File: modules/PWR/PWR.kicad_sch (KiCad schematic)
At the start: 18 parts, among them SW1 POWER ON, SW2 RESET, U1 74HC00

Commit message: pwr pcb
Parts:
- R1: value 150Ω -> 1kΩ
- R2: value 100Ω -> 1kΩ
- U1: value 74HC00 -> 74HCT00
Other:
- note added: "BUS RESET"
- note added: "I^{2}C SUPPORT"
- note added: "METERS"
- note added: "POWER AND DECOUPLING"
- note added: "POWER CONTROL"
- note added: "TURNS OFF THE STANDBY LED WHEN MAIN POWER IS ENABLED."
- title: PWR-CTRL -> PWR
- moved on the sheet: C1, C2, C3, D1, D2, JP1, MES1, MES2, MES3, MES4, R1, R2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

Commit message: minor PW PCB tweaks
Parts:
- SW1: value POWER ON -> PWR ON
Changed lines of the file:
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@@
 			)
 		)
-		(property "Value" "POWER ON"
+		(property "Value" "PWR ON"
 			(at 77.47 35.56 0)
 			(show_name no)

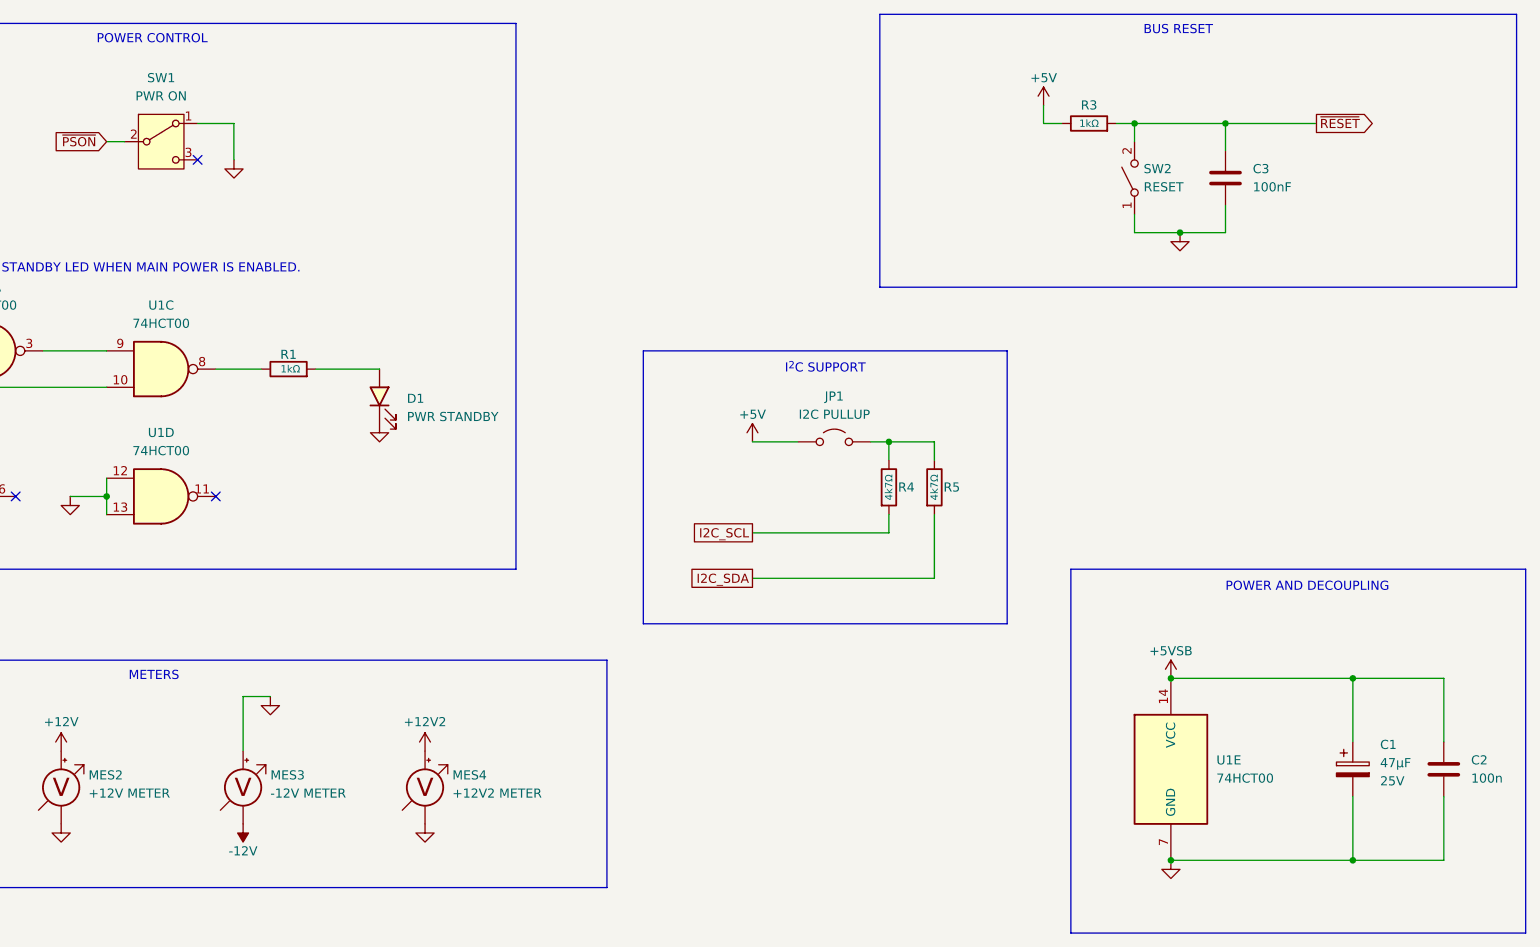
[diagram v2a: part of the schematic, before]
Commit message: version 1 of pwr module, power panel, & backplane pcb
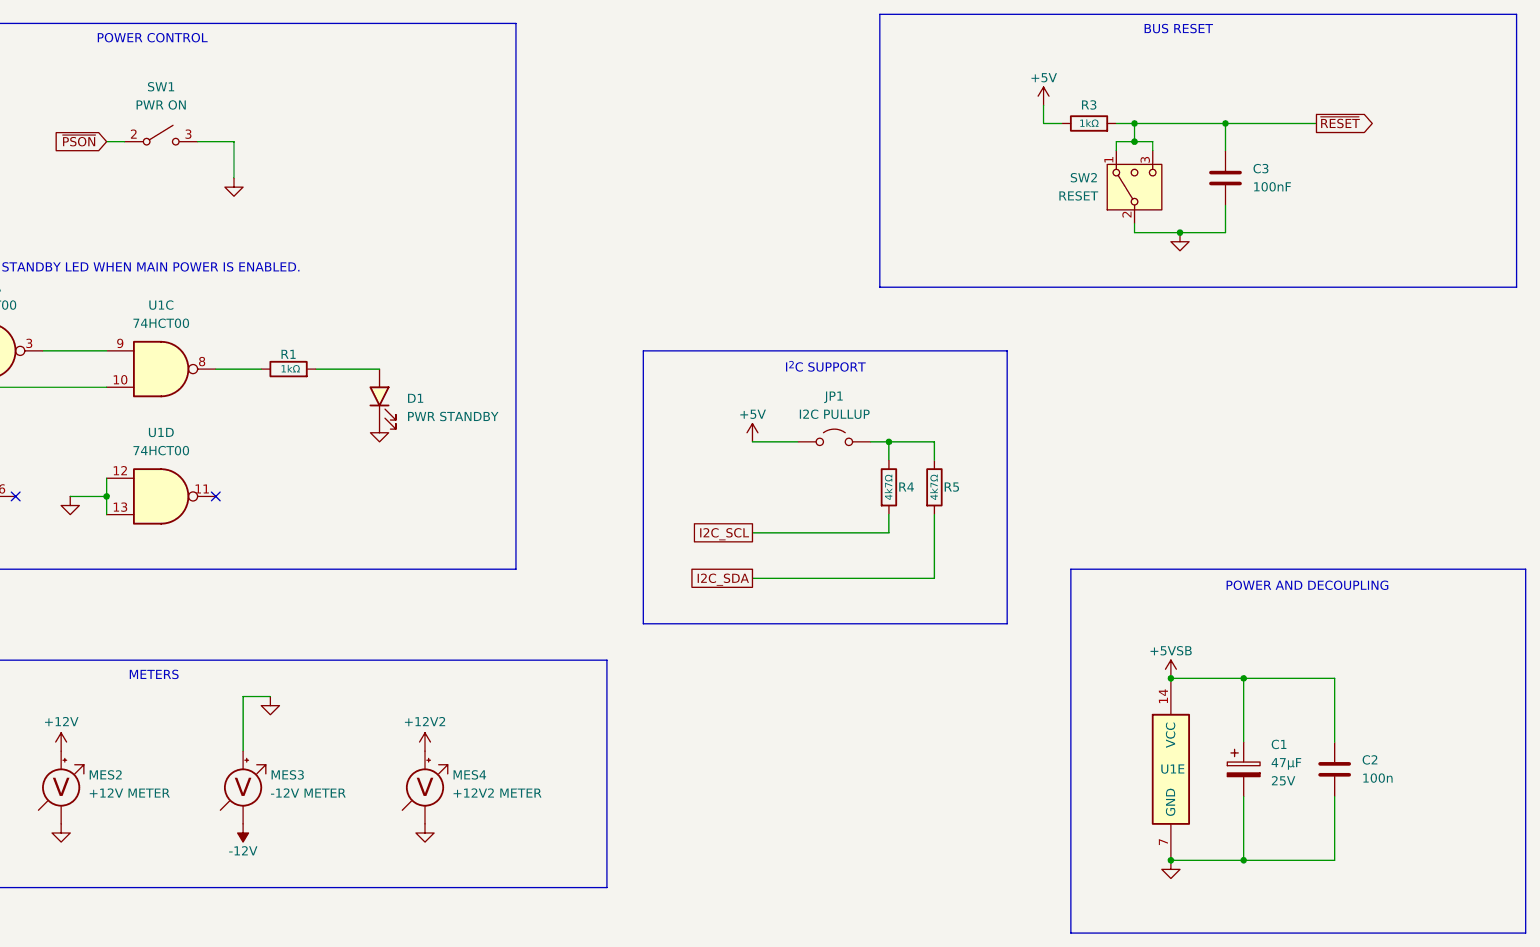
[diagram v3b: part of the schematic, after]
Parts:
- C1: footprint Capacitor_THT:CP_Radial_D5.0mm_P2.50mm -> FormantKO:CP_Radial_Tantal_P200mil
- D1, D2, MES1, MES2, MES3, MES4: footprint FormantKO:PanelConnector_1x02 -> IMNOTWOPR:PanelConnector_1x02
- JP1: footprint FormantKO:Jumper_1x02 -> IMNOTWOPR:Jumper_1x02
- SW1: footprint FormantKO:PanelConnector_1x02 -> IMNOTWOPR:PanelConnector_1x03; symbol Switch:SW_SPDT -> IMNOTWOPR:SW_SPST
- SW2: footprint FormantKO:PanelConnector_1x02 -> IMNOTWOPR:PanelConnector_1x03; symbol Switch:SW_SPST -> IMNOTWOPR:SW_SPDT_MSM
- U1: symbol 74xx:74HC00 -> IMNOTWOPR:74HCT00
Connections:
- net GND: now also SW1.3 (C), SW2.2 (3); no longer SW1.1 (A), SW2.1 (A)
- net ~{RESET}: now also SW2.1, SW2.3 (4); no longer SW2.2 (B)
- no-connect marks 3 -> 2
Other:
- moved on the sheet: C1, C2

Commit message: lib work and ben wip
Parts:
- removed R3: 1kΩ, IMNOTWOPR:R_Axial_DIN0207_P400mil, symbol IMNOTWOPR:R
- removed SW2: RESET, IMNOTWOPR:PanelConnector_1x03, symbol IMNOTWOPR:SW_SPDT_MSM
- added C1: 10n, IMNOTWOPR:C_Rect_P200mil, symbol IMNOTWOPR:C
- added C2: 1u, IMNOTWOPR:C_Rect_P200mil, symbol IMNOTWOPR:C
- added C6, C7: 100n, IMNOTWOPR:C_Rect_P200mil, symbol IMNOTWOPR:C
- added D2, D4: 1N4148, FormantKO:DO-35_P400mil, symbol IMNOTWOPR:1N4148
- added J1: CardConnector, IMNOTWOPR:SystemConector_Male, symbol IMNOTWOPR:CardConnector
- added MH1: CardBracket, IMNOTWOPR:CardBracket, symbol IMNOTWOPR:CardBracket
- added R2: 10k, IMNOTWOPR:R_Axial_DIN0207_P400mil, symbol IMNOTWOPR:R_Vertical
- added R3: 91k, IMNOTWOPR:R_Axial_DIN0207_P400mil, symbol IMNOTWOPR:R_Vertical
- added SW1: 1MS2T1B1M1QES, IMNOTWOPR:PanelConnector_1x03, symbol IMNOTWOPR:SW_SPST
- added U1: 74HCT14, IMNOTWOPR:DIP-14N, symbol IMNOTWOPR:74HCT14
- added U3: 555, IMNOTWOPR:DIP-8N, symbol IMNOTWOPR:555
- C3: value 100nF -> 10n
- C4: renamed from C1; footprint FormantKO:CP_Radial_Tantal_P200mil -> IMNOTWOPR:CP_Radial_Tantal_P100mil; Voltage 25V -> 35V
- D1: renamed from D2; footprint IMNOTWOPR:PanelConnector_1x02 -> IMNOTWOPR:LED_G_D5.0mm
- D3: renamed from D1; footprint IMNOTWOPR:PanelConnector_1x02 -> IMNOTWOPR:LED_D5.0mm
- JP1: footprint IMNOTWOPR:Jumper_1x02 -> (none)
- MES1, MES2, MES3, MES4: footprint IMNOTWOPR:PanelConnector_1x02 -> (none)
- SW2: renamed from SW1; value PWR ON -> 1MS1T1B1M1QES; Legend (none) -> POWER ON
- renumbered C2 to C5, R2 to R1, R1 to R4, R4 to R5, R5 to R6, U1 to U2
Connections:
- net +12V: now also J1.a3 (+12V), J1.a30 (+12V)
- net +12V2: now also J1.c3 (+12V2), J1.c30 (+12V2)
- net +5V: now also D2.1 (K), J1.a1 (+5V), J1.a2 (+5V), J1.a31 (+5V), J1.a32 (+5V), J1.b1 (+5V), J1.b32 (+5V), R2.2, R3.2, U3.4 (~{RST}), U3.8 (VCC)
- net +5VSB: now also C6.1, C7.1, J1.c1 (+5VSB), U1.14 (VCC)
- net -12V: now also J1.b3 (-12V), J1.b30 (-12V)
- net GND: now also C2.2, C6.2, C7.2, J1.b2 (GND), J1.b31 (GND), J1.c12 (GND), J1.c18 (GND), J1.c2 (GND), J1.c24 (GND), J1.c31 (GND), J1.c32 (GND), J1.c6 (GND), SW1.2 (B), U1.11, U1.13, U1.5, U1.7 (GND), U1.9, U3.1 (GND)
- net I2C_SCL: now also J1.c7 (I2C_SCL)
- net I2C_SDA: now also J1.c8 (I2C_SDA)
- net PWROK: now also J1.c5 (PWROK), U1.1
- net ~{PSON}: now also J1.c4 (~{PSON})
- net ~{RESET}: now also D4.1 (K), J1.b15 (~{RESET}); no longer C3.1
- new net: C1.1, U1.2
- new net: C1.2, D2.2 (A), R2.1, SW1.3 (C), U3.2 (TRIG)
- new net: C2.1, R3.1, U3.6 (THRES), U3.7 (DISCH)
- new net: U1.3, U3.3 (OUT)
- new net: C3.1, U3.5 (CONT)
- new net: D4.2 (A), U1.4
- no-connect marks 2 -> 75
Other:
- note added: "MANUAL & POWER ON RESET"
- note added: "≈ 100ms PULSE"
- note removed: "BUS RESET"
- moved on the sheet: C4, C5, D1, D3, JP1, MES1, MES2, MES3, MES4, R1, R4, R5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

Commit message: ben work; fixed logic issue with pwr; started lightman
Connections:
- net GND: no longer U2.4, U2.5
- net at U2.8: now also U2.4, U2.5; no longer R4.1
- net at U2.6: now also R4.1
- no-connect marks 75 -> 74
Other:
- moved on the sheet: D3, R4
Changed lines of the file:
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@@
 	)
 	(junction
-		(at 81.28 255.27)
+		(at 133.35 73.66)
 		(diameter 0)
 		(color 0 0 0 0)
@@
 	)
 	(no_connect
-		(at 96.52 255.27)
-	)
-	(no_connect
 		(at 30.48 163.83)
 	)
@@
 	(wire
 		(pts
-			(xy 91.44 76.2) (xy 120.65 76.2)
+			(xy 91.44 76.2) (xy 114.3 76.2)
 		)
 		(stroke
@@
 	(wire
 		(pts
-			(xy 111.76 71.12) (xy 120.65 71.12)
+			(xy 111.76 71.12) (xy 114.3 71.12)
 		)
 		(stroke
@@
 	(wire
 		(pts
-			(xy 78.74 255.27) (xy 81.28 255.27)
-		)
-		(stroke
-			(width 0)
-			(type default)
-		)
-	)
-	(wire
-		(pts
 			(xy 147.32 144.78) (xy 144.78 144.78)
 		)
@@
 	(wire
 		(pts
-			(xy 81.28 255.27) (xy 81.28 257.81)
+			(xy 133.35 73.66) (xy 133.35 76.2)
 		)
 		(stroke
@@
 	(wire
 		(pts
-			(xy 78.74 266.7) (xy 81.28 266.7)
+			(xy 129.54 73.66) (xy 133.35 73.66)
 		)
 		(stroke
@@
 	(wire
 		(pts
-			(xy 127 215.9) (xy 139.7 215.9)
+			(xy 78.74 266.7) (xy 81.28 266.7)
 		)
 		(stroke
@@
 	(wire
 		(pts
-			(xy 35.56 24.13) (xy 30.48 24.13)
+			(xy 127 215.9) (xy 139.7 215.9)
 		)
 		(stroke
@@
 	(wire
 		(pts
-			(xy 101.6 152.4) (xy 102.87 152.4)
+			(xy 35.56 24.13) (xy 30.48 24.13)
 		)
 		(stroke
@@
 	(wire
 		(pts
-			(xy 30.48 209.55) (xy 41.91 209.55)
+			(xy 101.6 152.4) (xy 102.87 152.4)
 		)
 		(stroke
@@
 	(wire
 		(pts
-			(xy 135.89 73.66) (xy 142.24 73.66)
+			(xy 30.48 209.55) (xy 41.91 209.55)
 		)
 		(stroke
@@
 	(wire
 		(pts
-			(xy 81.28 252.73) (xy 81.28 255.27)
+			(xy 133.35 71.12) (xy 133.35 73.66)
 		)
 		(stroke
@@
 	(wire
 		(pts
-			(xy 158.75 73.66) (xy 149.86 73.66)
+			(xy 160.02 73.66) (xy 156.21 73.66)
 		)
 		(stroke
@@
 	)
 	(symbol
-		(lib_id "power:GND")
-		(at 78.74 255.27 0)
-		(unit 1)
-		(body_style 1)
-		(exclude_from_sim no)
-		(in_bom yes)
-		(on_board yes)
-		(in_pos_files yes)
-		(dnp no)
-		(fields_autoplaced yes)
-		(property "Reference" "#PWR01"
-			(at 78.74 261.62 0)
-			(hide yes)
-			(show_name no)
-			(do_not_autoplace no)
-			(effects
-				(font
-					(size 1.27 1.27)
-				)
-			)
-		)
-		(property "Value" "GND"
-			(at 78.74 260.35 0)
-			(hide yes)
-			(show_name no)
-			(do_not_autoplace no)
-			(effects
-				(font
-					(size 1.27 1.27)
-				)
-			)
-		)
-		(property "Footprint" ""
-			(at 78.74 255.27 0)
-			(hide yes)
-			(show_name no)
-			(do_not_autoplace no)
-			(effects
-				(font
-					(size 1.27 1.27)
-				)
-			)
-		)
-		(property "Datasheet" ""
-			(at 78.74 255.27 0)
-			(hide yes)
-			(show_name no)
-			(do_not_autoplace no)
-			(effects
-				(font
-					(size 1.27 1.27)
-				)
-			)
-		)
-		(property "Description" "Power symbol creates a global label with name \"GND\" , ground"
-			(at 78.74 255.27 0)
-			(hide yes)
-			(show_name no)
-			(do_not_autoplace no)
-			(effects
-				(font
-					(size 1.27 1.27)
-				)
-			)
-		)
-		(pin "1"
-		)
-		(instances
-			(project "PWR"
-				(path "/e63e39d7-6ac0-4ffd-8aa3-1841a4541b55"
-					(reference "#PWR01")
-					(unit 1)
-				)
-			)
-		)
-	)
-	(symbol
 		(lib_id "IMNOTWOPR:LED_G")
 		(at 90.17 48.26 90)
@@
 	(symbol
 		(lib_id "IMNOTWOPR:74HCT00")
-		(at 128.27 73.66 0)
+		(at 121.92 73.66 0)
 		(unit 3)
 		(body_style 1)
@@
 		(fields_autoplaced yes)
 		(property "Reference" "U2"
-			(at 128.27 64.77 0)
+			(at 121.92 64.77 0)
 			(hide yes)
 			(show_name no)
@@
 		)
 		(property "Value" "74HCT00"
-			(at 128.27 67.31 0)
+			(at 121.92 67.31 0)
 			(hide yes)
 			(show_name no)
@@
 		)
 		(property "Footprint" "IMNOTWOPR:DIP-14N"
-			(at 128.27 73.66 0)
+			(at 121.92 73.66 0)
 			(hide yes)
 			(show_name no)
@@
 		)
 		(property "Datasheet" "http://www.ti.com/lit/gpn/sn74hc00"
-			(at 128.27 73.66 0)
+			(at 121.92 73.66 0)
 			(hide yes)
 			(show_name no)
@@
 		)
 		(property "Description" "quad 2-input NAND gate"
-			(at 128.27 73.66 0)
+			(at 121.92 73.66 0)
 			(hide yes)
 			(show_name no)
@@
 	(symbol
 		(lib_id "IMNOTWOPR:R")
-		(at 146.05 73.66 0)
+		(at 152.4 73.66 0)
 		(unit 1)
 		(body_style 1)
@@
 		(dnp no)
 		(property "Reference" "R4"
-			(at 146.05 72.39 0)
+			(at 152.4 72.39 0)
 			(show_name no)
 			(do_not_autoplace no)
@@
 		)
 		(property "Value" "1kΩ"
-			(at 146.304 73.66 0)
+			(at 152.654 73.66 0)
 			(show_name no)
 			(do_not_autoplace no)
@@
 		)
 		(property "Footprint" "IMNOTWOPR:R_Axial_DIN0207_P400mil"
-			(at 146.05 73.66 0)
+			(at 152.4 73.66 0)
 			(hide yes)
 			(show_name no)
@@
 		)
 		(property "Datasheet" ""
-			(at 146.05 73.66 90)
+			(at 152.4 73.66 90)
 			(hide yes)
 			(show_name no)
@@
 		)
 		(property "Description" "Resistor"
-			(at 146.05 73.66 0)
+			(at 152.4 73.66 0)
 			(hide yes)
 			(show_name no)
@@
 	(symbol
 		(lib_id "IMNOTWOPR:LED_R")
-		(at 158.75 77.47 90)
+		(at 160.02 77.47 90)
 		(unit 1)
 		(body_style 1)
@@
 		(fields_autoplaced yes)
 		(property "Reference" "D3"
-			(at 162.56 77.7874 90)
+			(at 163.83 77.7874 90)
 			(show_name no)
 			(do_not_autoplace no)
@@
 		)
 		(property "Value" "PWR STANDBY"
-			(at 162.56 80.3274 90)
+			(at 163.83 80.3274 90)
 			(show_name no)
 			(do_not_autoplace no)
@@
 		)
 		(property "Footprint" "IMNOTWOPR:LED_D5.0mm"
-			(at 158.75 77.47 0)
+			(at 160.02 77.47 0)
 			(hide yes)
 			(show_name no)
@@
 		)
 		(property "Datasheet" ""
-			(at 158.75 77.47 0)
+			(at 160.02 77.47 0)
 			(hide yes)
 			(show_name no)
@@
 		)
 		(property "Description" "Light emitting diode"
-			(at 158.75 77.47 0)
+			(at 160.02 77.47 0)
 			(hide yes)
 			(show_name no)
@@
 		)
 		(property "Sim.Pins" "1=K 2=A"
-			(at 158.75 77.47 0)
+			(at 160.02 77.47 0)
 			(hide yes)
 			(show_name no)
@@
 	(symbol
 		(lib_id "power:GND")
-		(at 158.75 81.28 0)
+		(at 160.02 81.28 0)
 		(unit 1)
 		(body_style 1)
@@
 		(fields_autoplaced yes)
 		(property "Reference" "#PWR012"
-			(at 158.75 87.63 0)
+			(at 160.02 87.63 0)
 			(hide yes)
 			(show_name no)
@@
 		)
 		(property "Value" "GND"
-			(at 158.75 86.36 0)
+			(at 160.02 86.36 0)
 			(hide yes)
 			(show_name no)
@@
 		)
 		(property "Footprint" ""
-			(at 158.75 81.28 0)
+			(at 160.02 81.28 0)
 			(hide yes)
 			(show_name no)
@@
 		)
 		(property "Datasheet" ""
-			(at 158.75 81.28 0)
+			(at 160.02 81.28 0)
 			(hide yes)
 			(show_name no)
@@
 		)
 		(property "Description" "Power symbol creates a global label with name \"GND\" , ground"
-			(at 158.75 81.28 0)
+			(at 160.02 81.28 0)
 			(hide yes)
 			(show_name no)
@@
 	(symbol
 		(lib_id "IMNOTWOPR:74HCT00")
-		(at 88.9 255.27 0)
+		(at 140.97 73.66 0)
 		(unit 2)
 		(body_style 1)
@@
 		(fields_autoplaced yes)
 		(property "Reference" "U2"
-			(at 88.9 246.38 0)
+			(at 140.97 64.77 0)
 			(hide yes)
 			(show_name no)
@@
 		)
 		(property "Value" "74HCT00"
-			(at 88.9 248.92 0)
+			(at 140.97 67.31 0)
 			(hide yes)
 			(show_name no)
@@
 		)
 		(property "Footprint" "IMNOTWOPR:DIP-14N"
-			(at 88.9 255.27 0)
+			(at 140.97 73.66 0)
 			(hide yes)
 			(show_name no)
@@
 		)
 		(property "Datasheet" "http://www.ti.com/lit/gpn/sn74hc00"
-			(at 88.9 255.27 0)
+			(at 140.97 73.66 0)
 			(hide yes)
 			(show_name no)
@@
 		)
 		(property "Description" "quad 2-input NAND gate"
-			(at 88.9 255.27 0)
+			(at 140.97 73.66 0)
 			(hide yes)
 			(show_name no)

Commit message: lightman pcb
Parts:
- removed JP1: I2C PULLUP, symbol Jumper:Jumper_2_Open
- removed R5, R6: 4k7Ω, IMNOTWOPR:R_Axial_DIN0207_P400mil, symbol IMNOTWOPR:R
- D1: footprint IMNOTWOPR:LED_G_D5.0mm -> IMNOTWOPR:Wire_LED
- D3: footprint IMNOTWOPR:LED_D5.0mm -> IMNOTWOPR:Wire_LED
- MES1, MES2, MES3: footprint (none) -> IMNOTWOPR:Wire_Meter
- MES4: value +12V2 METER -> IMNOTWOPR:Wire_Meter; footprint (none) -> IMNOTWOPR:Wire_Meter
- SW1: footprint IMNOTWOPR:PanelConnector_1x03 -> IMNOTWOPR:Wire_SW_SPDT
- SW2: footprint IMNOTWOPR:PanelConnector_1x03 -> IMNOTWOPR:Wire_SW_SPST_23
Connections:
- net +5V: no longer D2.1 (K), R2.2, R3.2, U3.4 (~{RST}), U3.8 (VCC)
- net +5VSB: now also D2.1 (K), R2.2, R3.2, U3.4 (~{RST}), U3.8 (VCC)
- net I2C_SCL: no longer names the net of J1.c7 (I2C_SCL)
- net I2C_SDA: no longer names the net of J1.c8 (I2C_SDA)
- no-connect marks 74 -> 76
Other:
- note removed: "I^{2}C SUPPORT"
- moved on the sheet: J1B
